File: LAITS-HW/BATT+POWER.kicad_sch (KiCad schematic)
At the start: 60 parts, among them SW601 SW_SPDT, U601 NCV8164ASN180T1G, U602 AP62301WU-7, U603 MAX77960BEFV12+

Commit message: generate IBOM
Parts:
- R619: Place (none) -> DNP
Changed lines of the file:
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@@
+      (effects (font (size 1.27 1.27)) hide)
+    )
+    (property "Place" "DNP" (id 4) (at 196.85 106.68 0)
       (effects (font (size 1.27 1.27)) hide)
     )

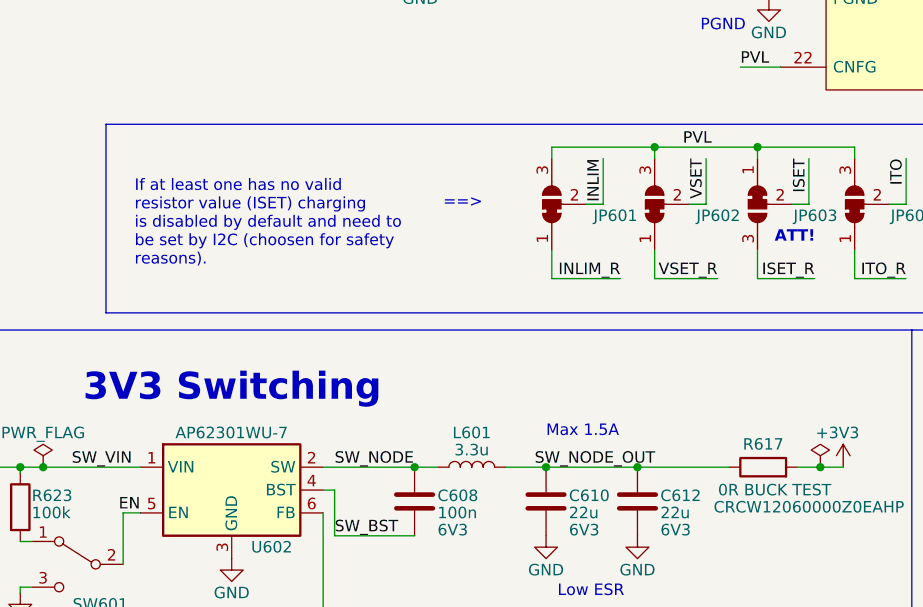
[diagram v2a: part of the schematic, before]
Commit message: Patch 1.0.1
Bug:

 - Changed U602 footprint from TSOT26 to SOT563 in order to reflect pin assignment.

Small bugs:

 - Missing silkscreen for SMD leds info (3V3, RX, TX)
 - DS18B20 silkscreen now reflect horizontal placement
 - Rotated and modified the pinout of the jumper JP603 so now it's clear that it is connected different in respect to JP601, JP602, JP604
 - Made visible the dot for the placement of U602
 - Made visible dot for placement D603 and D605
 - Added I2C info on Silkscreen for I2C Pull-up resistors
 - Add info on Sch for USB-C Shield connection
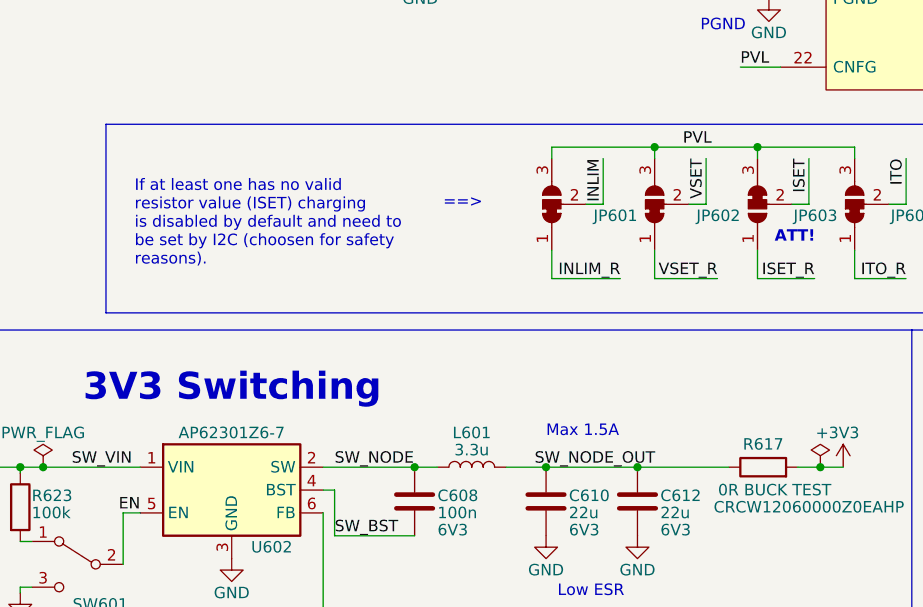
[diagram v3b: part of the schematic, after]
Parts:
- JP603: symbol Jumper:SolderJumper_3_Bridged12 -> LAITS-LIB:SolderJumper_3_Bridged32
- U602: value AP62301WU-7 -> AP62301Z6-7; footprint Package_TO_SOT_SMD:TSOT-23-6 -> LAITS-LIB:LAITS-SOT-563
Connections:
- net ISET_R: now also JP603.1 (A); no longer JP603.3 (B)
- net PVL: now also JP603.3 (B); no longer JP603.1 (A)
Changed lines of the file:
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@@
     (title "BATT")
     (date "2022-07-14")
-    (rev "1.0")
+    (rev "1.0.1")
     (company "Simone Tollardo")
   )
@@
     (in_bom yes) (on_board yes)
     (property "Reference" "U602" (id 0) (at 104.775 144.78 0))
-    (property "Value" "AP62301WU-7" (id 1) (at 100.33 132.08 0))
-    (property "Footprint" "Package_TO_SOT_SMD:TSOT-23-6" (id 2) (at 100.33 128.27 0)
+    (property "Value" "AP62301Z6-7" (id 1) (at 100.33 132.08 0))
+    (property "Footprint" "LAITS-LIB:LAITS-SOT-563" (id 2) (at 100.33 128.27 0)
       (effects (font (size 1.27 1.27)) hide)
     )
@@
     (pin "2")
   )
-  (symbol (lib_id "Jumper:SolderJumper_3_Bridged12") (at 158.75 106.68 90) (mirror x) (unit 1)
+  (symbol (lib_id "LAITS-LIB:SolderJumper_3_Bridged32") (at 158.75 106.68 90) (mirror x) (unit 1)
     (in_bom no) (on_board yes)
     (property "Reference" "JP603" (id 0) (at 167.64 107.95 90)

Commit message: Fixed a minor bug in the assignment of SDA0 and SCL0 pins, doesn't affect Hardware, swap in firmware
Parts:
- U602: symbol LAITS-LIB:AP62301WU-7 -> LAITS-LIB:AP62301Z6-7
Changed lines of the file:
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@@
   (title_block
     (title "BATT")
-    (date "2022-07-14")
-    (rev "1.0.1")
+    (date "2022-08-11")
+    (rev "1.0.2")
     (company "Simone Tollardo")
   )
@@
     (pin "2")
   )
-  (symbol (lib_id "LAITS-LIB:AP62301WU-7") (at 100.33 138.43 0) (unit 1)
+  (symbol (lib_id "LAITS-LIB:AP62301Z6-7") (at 100.33 138.43 0) (unit 1)
     (in_bom yes) (on_board yes)
     (property "Reference" "U602" (id 0) (at 104.775 144.78 0))

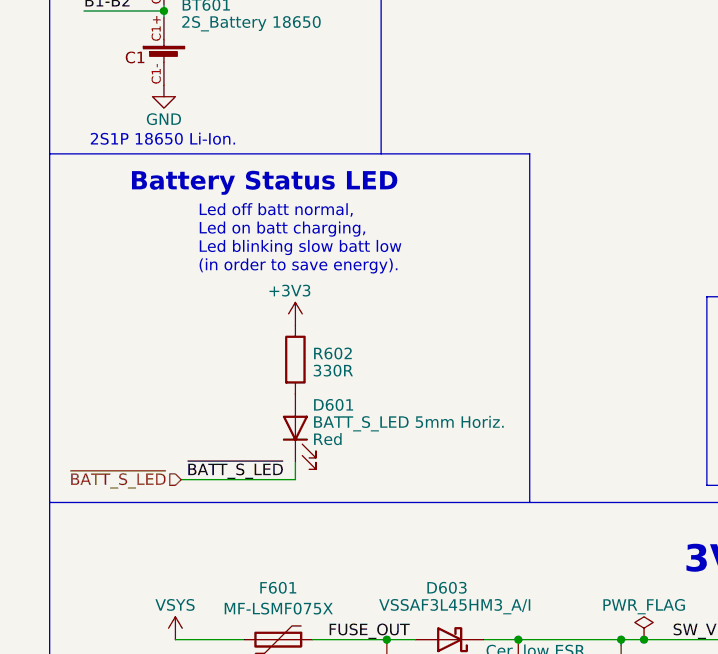
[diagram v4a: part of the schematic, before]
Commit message: Now LAITS notify charge state also when turned off
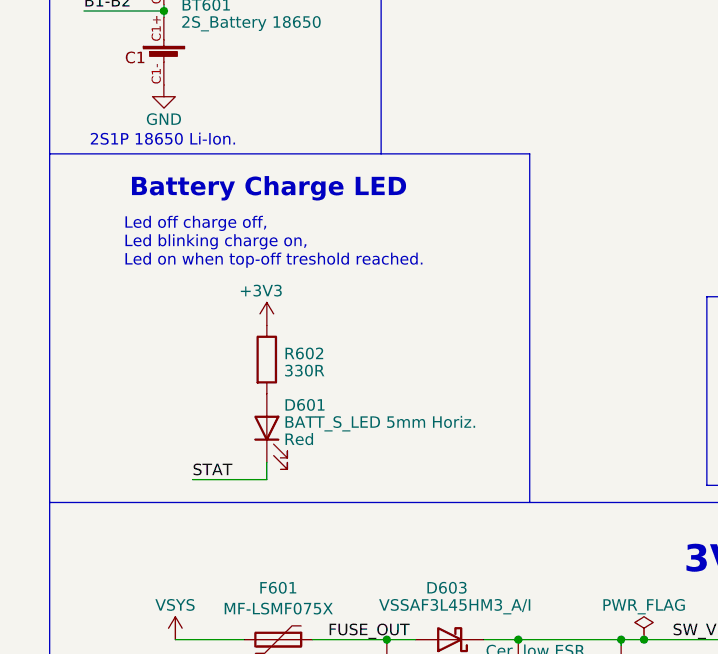
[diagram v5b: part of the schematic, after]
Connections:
- net ~{BATT_S_LED} is gone; now on net STAT: D601.1 (K)
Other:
- note added: "Battery Charge LED"
- note added: "Led off charge off, Led blinking charge on, Led on when top-off treshold reached."
- note removed: "Battery Status LED"
- note removed: "Led off batt normal, Led on batt charging, Led blinking slow batt low (in order to save energy)."
- moved on the sheet: D601, R602
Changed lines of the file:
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@@
   (title_block
     (title "BATT")
-    (date "2022-08-11")
-    (rev "1.0.2")
+    (date "2022-08-12")
+    (rev "1.0.3")
     (company "Simone Tollardo")
   )
@@
     (stroke (width 0) (type default) (color 0 0 0 0))
   )
-  (wire (pts (xy 40.64 116.205) (xy 40.64 118.11))
+  (wire (pts (xy 37.465 116.205) (xy 37.465 118.11))
     (stroke (width 0) (type default) (color 0 0 0 0))
   )
@@
     (stroke (width 0) (type default) (color 0 0 0 0))
   )
-  (wire (pts (xy 27.94 118.11) (xy 40.64 118.11))
+  (wire (pts (xy 29.21 118.11) (xy 37.465 118.11))
     (stroke (width 0) (type default) (color 0 0 0 0))
   )
@@
     (effects (font (size 1.27 1.27)) (justify left bottom))
   )
-  (text "Led off batt normal,\nLed on batt charging,\nLed blinking slow batt low\n(in order to save energy)."
-    (at 29.845 95.25 0)
+  (text "Led off charge off,\nLed blinking charge on,\nLed on when top-off treshold reached."
+    (at 21.59 94.615 0)
     (effects (font (size 1.27 1.27)) (justify left bottom))
   )
@@
     (effects (font (size 1.27 1.27)) (justify left bottom))
   )
-  (text "Battery Status LED" (at 22.225 86.36 0)
+  (text "Battery Charge LED" (at 22.225 86.995 0)
     (effects (font (size 2.032 2.032) (thickness 0.6) bold) (justify left bottom))
   )
@@
     (effects (font (size 1.27 1.27)) (justify left bottom))
   )
+  (label "STAT" (at 29.21 118.11 0)
+    (effects (font (size 1.27 1.27)) (justify left bottom))
+  )
   (label "VSET" (at 153.035 101.6 270)
     (effects (font (size 1.27 1.27)) (justify right bottom))
@@
     (effects (font (size 1.27 1.27)) (justify left bottom))
   )
-  (label "~{BATT_S_LED}" (at 28.575 118.11 0)
-    (effects (font (size 1.27 1.27)) (justify left bottom))
-  )
   (label "DISQBAT" (at 153.67 66.04 0)
     (effects (font (size 1.27 1.27)) (justify left bottom))
@@
     (effects (font (size 1.27 1.27)) (justify right))
   )
-  (hierarchical_label "~{BATT_S_LED}" (shape input) (at 27.94 118.11 180)
-    (effects (font (size 1.27 1.27)) (justify right))
-  )
   (hierarchical_label "SDA1" (shape bidirectional) (at 68.58 53.34 180)
     (effects (font (size 1.27 1.27)) (justify right))
@@
     (pin "1")
   )
-  (symbol (lib_id "Device:R") (at 40.64 104.775 0) (unit 1)
+  (symbol (lib_id "Device:R") (at 37.465 104.775 0) (unit 1)
     (in_bom yes) (on_board yes)
-    (property "Reference" "R602" (id 0) (at 42.545 104.14 0)
+    (property "Reference" "R602" (id 0) (at 39.37 104.14 0)
       (effects (font (size 1.27 1.27)) (justify left))
     )
-    (property "Value" "330R" (id 1) (at 42.545 106.045 0)
+    (property "Value" "330R" (id 1) (at 39.37 106.045 0)
       (effects (font (size 1.27 1.27)) (justify left))
     )
-    (property "Footprint" "Resistor_SMD:R_0603_1608Metric" (id 2) (at 38.862 104.775 90)
+    (property "Footprint" "Resistor_SMD:R_0603_1608Metric" (id 2) (at 35.687 104.775 90)
       (effects (font (size 1.27 1.27)) hide)
     )
-    (property "Datasheet" "~" (id 3) (at 40.64 104.775 0)
+    (property "Datasheet" "~" (id 3) (at 37.465 104.775 0)
       (effects (font (size 1.27 1.27)) hide)
     )
@@
     (pin "1")
   )
-  (symbol (lib_id "Device:LED") (at 40.64 112.395 90) (unit 1)
+  (symbol (lib_id "Device:LED") (at 37.465 112.395 90) (unit 1)
     (in_bom yes) (on_board yes)
-    (property "Reference" "D601" (id 0) (at 42.545 109.855 90)
+    (property "Reference" "D601" (id 0) (at 39.37 109.855 90)
       (effects (font (size 1.27 1.27)) (justify right))
     )
-    (property "Value" "BATT_S_LED 5mm Horiz." (id 1) (at 42.545 111.76 90)
+    (property "Value" "BATT_S_LED 5mm Horiz." (id 1) (at 39.37 111.76 90)
       (effects (font (size 1.27 1.27)) (justify right))
     )
-    (property "Footprint" "LED_THT:LED_D5.0mm_Horizontal_O3.81mm_Z3.0mm" (id 2) (at 40.64 112.395 0)
+    (property "Footprint" "LED_THT:LED_D5.0mm_Horizontal_O3.81mm_Z3.0mm" (id 2) (at 37.465 112.395 0)
       (effects (font (size 1.27 1.27)) hide)
     )
-    (property "Datasheet" "~" (id 3) (at 40.64 112.395 0)
+    (property "Datasheet" "~" (id 3) (at 37.465 112.395 0)
       (effects (font (size 1.27 1.27)) hide)
     )
-    (property "Color" "Red" (id 4) (at 42.545 113.665 90)
+    (property "Color" "Red" (id 4) (at 39.37 113.665 90)
       (effects (font (size 1.27 1.27)) (justify right))
     )
@@
     (pin "2")
   )
-  (symbol (lib_id "power:+3V3") (at 40.64 100.965 0) (unit 1)
+  (symbol (lib_id "power:+3V3") (at 37.465 100.965 0) (unit 1)
     (in_bom yes) (on_board yes)
-    (property "Reference" "#PWR0606" (id 0) (at 40.64 104.775 0)
+    (property "Reference" "#PWR0606" (id 0) (at 37.465 104.775 0)
       (effects (font (size 1.27 1.27)) hide)
     )
-    (property "Value" "+3V3" (id 1) (at 40.005 97.155 0))
-    (property "Footprint" "" (id 2) (at 40.64 100.965 0)
+    (property "Value" "+3V3" (id 1) (at 36.83 97.155 0))
+    (property "Footprint" "" (id 2) (at 37.465 100.965 0)
       (effects (font (size 1.27 1.27)) hide)
     )
-    (property "Datasheet" "" (id 3) (at 40.64 100.965 0)
+    (property "Datasheet" "" (id 3) (at 37.465 100.965 0)
       (effects (font (size 1.27 1.27)) hide)
     )
